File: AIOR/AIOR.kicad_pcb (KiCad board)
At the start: 2 copper layers, 85 x 56.5 mm, 35 parts, among them J1 Conn_01x06, J2 Conn_01x02, P1 CONN_02X20, P2 CONN_01X02, P3 CONN_01X04, P8 CONN_01X02, P9 CONN_01X04, U1 MCP2517FD, U3 P82B715, U4 SI8641-SOIC, Y1 4MHz

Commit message: wip
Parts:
- removed C6, C7, C8: 100nF, Capacitors_SMD:C_0805_HandSoldering
- removed J2: Conn_01x02, Pin_Headers:Pin_Header_Straight_1x02_Pitch2.54mm
- removed R4: 4k7, Resistors_SMD:R_0805_HandSolderingII
- removed R7: 120, Resistors_SMD:R_1206_HandSolderingII
- removed R8: 0, Resistors_SMD:R_0805_HandSolderingII
- removed R9: 50, Resistors_SMD:R_0805_HandSolderingII
- removed U3: P82B715, w_smd_dil:so-8
- added C10: 100nF, Capacitor_SMD:C_0805_2012Metric_Pad1.15x1.40mm_HandSolder, F.Cu at (109.6, 53.5)
- added C20: 100nF, Capacitor_SMD:C_0805_2012Metric_Pad1.15x1.40mm_HandSolder, F.Cu at (98.5, 63.2)
- added C21: 100nF, Capacitor_SMD:C_0805_2012Metric_Pad1.15x1.40mm_HandSolder, F.Cu at (126.4, 34.8)
- added C22: 10uF, Capacitor_SMD:C_Elec_5x5.8, F.Cu at (112.0, 45.6)
- added C23: 100nF, Capacitor_SMD:C_0805_2012Metric_Pad1.15x1.40mm_HandSolder, F.Cu at (121.6, 36.0)
- added C24: 100nF, Capacitor_SMD:C_0805_2012Metric_Pad1.15x1.40mm_HandSolder, F.Cu at (98.5, 66.1)
- added C25: 100nF, Capacitor_SMD:C_0805_2012Metric_Pad1.15x1.40mm_HandSolder, F.Cu at (138.3, 22.7)
- added C26: 100nF, Capacitor_SMD:C_0805_2012Metric_Pad1.15x1.40mm_HandSolder, F.Cu at (118.6, 43.0)
- added C27: 22pF, Capacitor_SMD:C_0805_2012Metric_Pad1.15x1.40mm_HandSolder, F.Cu at (121.6, 38.9)
- added C28: 22pF, Capacitor_SMD:C_0805_2012Metric_Pad1.15x1.40mm_HandSolder, F.Cu at (138.3, 19.7)
- added C29: 100nF, Capacitor_SMD:C_0805_2012Metric_Pad1.15x1.40mm_HandSolder, F.Cu at (147.6, 11.1)
- added C30: 100nF, Capacitor_SMD:C_0805_2012Metric_Pad1.15x1.40mm_HandSolder, F.Cu at (90.7, 67.7)
- added C31: 100nF, Capacitor_SMD:C_0805_2012Metric_Pad1.15x1.40mm_HandSolder, F.Cu at (126.4, 31.8)
- added C40: 100nF, Capacitor_SMD:C_0805_2012Metric_Pad1.15x1.40mm_HandSolder, F.Cu at (103.7, 55.1)
- added C41: 100nF, Capacitor_SMD:C_0805_2012Metric_Pad1.15x1.40mm_HandSolder, F.Cu at (145.4, 34.7)
- added C42: 100nF, Capacitor_SMD:C_0805_2012Metric_Pad1.15x1.40mm_HandSolder, F.Cu at (122.7, 60.7)
- added C43: 100nF, Capacitor_SMD:C_0805_2012Metric_Pad1.15x1.40mm_HandSolder, F.Cu at (114.8, 78.7)
- added C44: 100nF, Capacitor_SMD:C_0805_2012Metric_Pad1.15x1.40mm_HandSolder, F.Cu at (110.2, 78.7)
- added C45: 1nF, Capacitor_SMD:C_0805_2012Metric_Pad1.15x1.40mm_HandSolder, F.Cu at (133.4, 49.5)
- added C46: 100nF, Capacitor_SMD:C_0805_2012Metric_Pad1.15x1.40mm_HandSolder, F.Cu at (150.1, 31.8)
- added C70: 100nF, Capacitor_SMD:C_0805_2012Metric_Pad1.15x1.40mm_HandSolder, F.Cu at (128.6, 52.5)
- added C71: 1nF, Capacitor_SMD:C_0805_2012Metric_Pad1.15x1.40mm_HandSolder, F.Cu at (137.6, 43.3)
- added C72: 47pF, Capacitor_SMD:C_0805_2012Metric_Pad1.15x1.40mm_HandSolder, F.Cu at (122.7, 57.8)
- added C81: 100nF, Capacitor_SMD:C_0805_2012Metric_Pad1.15x1.40mm_HandSolder, F.Cu at (133.4, 46.6)
- added C82: 100nF, Capacitor_SMD:C_0805_2012Metric_Pad1.15x1.40mm_HandSolder, F.Cu at (119.2, 63.7)
- added C83: 100nF, Capacitor_SMD:C_0805_2012Metric_Pad1.15x1.40mm_HandSolder, F.Cu at (150.2, 28.8)
- added C84: 100nF, Capacitor_SMD:C_0805_2012Metric_Pad1.15x1.40mm_HandSolder, F.Cu at (114.4, 65.3)
- added C85: 100nF, Capacitor_SMD:C_0805_2012Metric_Pad1.15x1.40mm_HandSolder, F.Cu at (117.9, 60.7)
- added C86: 100nF, Capacitor_SMD:C_0805_2012Metric_Pad1.15x1.40mm_HandSolder, F.Cu at (137.6, 40.4)
- added C90: 100nF, Capacitor_SMD:C_0805_2012Metric_Pad1.15x1.40mm_HandSolder, F.Cu at (140.6, 37.4)
- added C91: 47pF, Capacitor_SMD:C_0805_2012Metric_Pad1.15x1.40mm_HandSolder, F.Cu at (140.7, 28.6)
- added C92: 47pF, Capacitor_SMD:C_0805_2012Metric_Pad1.15x1.40mm_HandSolder, F.Cu at (145.4, 37.7)
- added C93: 1nF, Capacitor_SMD:C_0805_2012Metric_Pad1.15x1.40mm_HandSolder, F.Cu at (126.3, 37.7)
- added C94: 1nF, Capacitor_SMD:C_0805_2012Metric_Pad1.15x1.40mm_HandSolder, F.Cu at (147.6, 14.1)
- added C95: 1nF, Capacitor_SMD:C_0805_2012Metric_Pad1.15x1.40mm_HandSolder, F.Cu at (108.4, 59.4)
- added C96: 560pF, Capacitor_SMD:C_0805_2012Metric_Pad1.15x1.40mm_HandSolder, F.Cu at (114.3, 53.5)
- added C97: 1nF, Capacitor_SMD:C_0805_2012Metric_Pad1.15x1.40mm_HandSolder, F.Cu at (152.3, 14.1)
- added C98: 1nF, Capacitor_SMD:C_0805_2012Metric_Pad1.15x1.40mm_HandSolder, F.Cu at (108.4, 56.5)
- added C99: 1nF, Capacitor_SMD:C_0805_2012Metric_Pad1.15x1.40mm_HandSolder, F.Cu at (147.8, 17.0)
- added D20: BAT43, Diode_SMD:D_SOD-323_HandSoldering, F.Cu at (85.8, 67.7)
- added D21: LED, LED_SMD:LED_0805_2012Metric_Pad1.15x1.40mm_HandSolder, F.Cu at (126.4, 28.8)
- added D70: LED, LED_SMD:LED_0805_2012Metric_Pad1.15x1.40mm_HandSolder, F.Cu at (109.6, 50.5)
- added D71: LED, LED_SMD:LED_0805_2012Metric_Pad1.15x1.40mm_HandSolder, F.Cu at (131.2, 28.3)
- added D90: 1N4148W, Diode_SMD:D_SOD-123, F.Cu at (104.3, 52.0)
- added D91: 1N4148W, Diode_SMD:D_SOD-123, F.Cu at (104.3, 48.6)
- added J20: Conn_01x04, Connector_PinHeader_2.54mm:PinHeader_1x04_P2.54mm_Vertical, F.Cu at (82.3, 29.8)
- added J30: Conn_01x01, Connector:Banana_Jack_1Pin, F.Cu at (167.1, 121.5)
- added J31: Conn_01x01, Connector:Banana_Jack_1Pin, F.Cu at (153.9, 121.4)
- added J50: Conn_01x02, Connector_PinHeader_2.54mm:PinHeader_1x02_P2.54mm_Vertical, F.Cu at (133.6, 20.6)
- added J70: Conn_01x01, Connector_PinHeader_2.54mm:PinHeader_1x01_P2.54mm_Vertical, F.Cu at (150.1, 38.5)
- added J81: Conn_01x06, Connector_PinHeader_2.54mm:PinHeader_1x06_P2.54mm_Horizontal, F.Cu at (132.8, 107.4)
- added J82: 5V 12V, Connector_PinHeader_2.54mm:PinHeader_1x03_P2.54mm_Vertical, F.Cu at (110.4, 34.8)
- added J90: Conn_01x03, Connector_PinHeader_2.54mm:PinHeader_1x03_P2.54mm_Vertical, F.Cu at (78.4, 42.0)
- added P50: Xpressnet, w_conn_jst-ph:s4b-ph-kl, F.Cu at (119.2, 11.8)
- added P60: Selectrix, w_conn_jst-ph:s4b-ph-kl, F.Cu at (102.4, 25.6)
- added P70: LOCONET, w_conn_jst-ph:s4b-ph-kl, F.Cu at (40.5, 74.0)
- added Q60: BC817, Package_TO_SOT_SMD:SOT-23_Handsoldering, F.Cu at (92.9, 64.0)
- added Q70: BC817, Package_TO_SOT_SMD:SOT-23_Handsoldering, F.Cu at (53.8, 74.7)
- added Q90: BC857, Package_TO_SOT_SMD:SOT-23_Handsoldering, F.Cu at (116.0, 39.3)
- added Q91: BC857, Package_TO_SOT_SMD:SOT-23_Handsoldering, F.Cu at (116.0, 34.7)
- added R20: 3k3, Resistor_SMD:R_0805_2012Metric_Pad1.15x1.40mm_HandSolder, F.Cu at (104.9, 66.9)
- added R21: 1k, Resistor_SMD:R_0805_2012Metric_Pad1.15x1.40mm_HandSolder, F.Cu at (147.8, 25.9)
- added R22: 3k3, Resistor_SMD:R_0805_2012Metric_Pad1.15x1.40mm_HandSolder, F.Cu at (119.1, 54.8)
- added R23: 3k3, Resistor_SMD:R_0805_2012Metric_Pad1.15x1.40mm_HandSolder, F.Cu at (123.4, 44.8)
- added R24: 18k, Resistor_SMD:R_0805_2012Metric_Pad1.15x1.40mm_HandSolder, F.Cu at (132.9, 40.7)
- added R25: 4k7, Resistor_SMD:R_0805_2012Metric_Pad1.15x1.40mm_HandSolder, F.Cu at (140.6, 34.5)
- added R30: 0, Resistor_SMD:R_0805_2012Metric_Pad1.15x1.40mm_HandSolder, F.Cu at (123.9, 50.7)
- added R31: 10k, Resistor_SMD:R_0805_2012Metric_Pad1.15x1.40mm_HandSolder, F.Cu at (152.5, 22.9)
- added R32: 3k3, Resistor_SMD:R_0805_2012Metric_Pad1.15x1.40mm_HandSolder, F.Cu at (113.2, 62.4)
- added R33: 4k7, Resistor_SMD:R_0805_2012Metric_Pad1.15x1.40mm_HandSolder, F.Cu at (123.9, 47.8)
- added R34: 100, Resistor_SMD:R_0805_2012Metric_Pad1.15x1.40mm_HandSolder, F.Cu at (132.9, 43.6)
- added R35: 100, Resistor_SMD:R_0805_2012Metric_Pad1.15x1.40mm_HandSolder, F.Cu at (145.5, 28.8)
- added R36: 4k7, Resistor_SMD:R_0805_2012Metric_Pad1.15x1.40mm_HandSolder, F.Cu at (109.7, 65.3)
- added R37: 0, Resistor_SMD:R_0805_2012Metric_Pad1.15x1.40mm_HandSolder, F.Cu at (123.9, 53.7)
- added R40: 470, Resistor_SMD:R_0805_2012Metric_Pad1.15x1.40mm_HandSolder, F.Cu at (128.6, 49.5)
- added R400: 3k3, Resistor_SMD:R_0805_2012Metric_Pad1.15x1.40mm_HandSolder, F.Cu at (154.9, 31.8)
- added R401: 3k3, Resistor_SMD:R_0805_2012Metric_Pad1.15x1.40mm_HandSolder, F.Cu at (147.8, 22.9)
- added R41: 3k3, Resistor_SMD:R_0805_2012Metric_Pad1.15x1.40mm_HandSolder, F.Cu at (152.5, 25.9)
- added R42: 470, Resistor_SMD:R_0805_2012Metric_Pad1.15x1.40mm_HandSolder, F.Cu at (145.4, 31.8)
- added R43: 3k3, Resistor_SMD:R_0805_2012Metric_Pad1.15x1.40mm_HandSolder, F.Cu at (128.6, 46.6)
- added R44: 1k, Resistor_SMD:R_0805_2012Metric_Pad1.15x1.40mm_HandSolder, F.Cu at (131.1, 37.7)
- added R45: 1k, Resistor_SMD:R_0805_2012Metric_Pad1.15x1.40mm_HandSolder, F.Cu at (138.3, 25.6)
- added R46: 1k, Resistor_SMD:R_0805_2012Metric_Pad1.15x1.40mm_HandSolder, F.Cu at (118.6, 46.0)
- added R47: 1k, Resistor_SMD:R_0805_2012Metric_Pad1.15x1.40mm_HandSolder, F.Cu at (152.3, 11.1)
- added R48: 0, Resistor_SMD:R_0805_2012Metric_Pad1.15x1.40mm_HandSolder, F.Cu at (123.4, 41.9)
- added R49: 0, Resistor_SMD:R_0805_2012Metric_Pad1.15x1.40mm_HandSolder, F.Cu at (119.1, 48.9)
- added R50: 470, Resistor_SMD:R_0805_2012Metric_Pad1.15x1.40mm_HandSolder, F.Cu at (100.2, 69.1)
- added R51: 470, Resistor_SMD:R_0805_2012Metric_Pad1.15x1.40mm_HandSolder, F.Cu at (103.7, 58.1)
- added R52: 120, Resistor_SMD:R_1206_3216Metric_Pad1.42x1.75mm_HandSolder, F.Cu at (104.4, 45.3)
- added R60: 27k, Resistor_SMD:R_0805_2012Metric_Pad1.15x1.40mm_HandSolder, F.Cu at (152.5, 17.0)
- added R61: 27k, Resistor_SMD:R_0805_2012Metric_Pad1.15x1.40mm_HandSolder, F.Cu at (128.6, 55.4)
- added R62: 120, Resistor_SMD:R_0805_2012Metric_Pad1.15x1.40mm_HandSolder, F.Cu at (147.8, 20.0)
- added R63: 1k, Resistor_SMD:R_0805_2012Metric_Pad1.15x1.40mm_HandSolder, F.Cu at (155.0, 28.8)
- added R700: 12, Resistor_SMD:R_1206_3216Metric_Pad1.42x1.75mm_HandSolder, F.Cu at (57.6, 69.2)
- added R701: 12, Resistor_SMD:R_1206_3216Metric_Pad1.42x1.75mm_HandSolder, F.Cu at (51.6, 69.2)
- added R702: 47k, Resistor_SMD:R_0805_2012Metric_Pad1.15x1.40mm_HandSolder, F.Cu at (133.4, 52.5)
- added R703: 150k, Resistor_SMD:R_0805_2012Metric_Pad1.15x1.40mm_HandSolder, F.Cu at (142.4, 40.6)
- added R71: 2k2, Resistor_SMD:R_0805_2012Metric_Pad1.15x1.40mm_HandSolder, F.Cu at (150.1, 34.7)
- added R72: 1k, Resistor_SMD:R_0805_2012Metric_Pad1.15x1.40mm_HandSolder, F.Cu at (138.1, 46.3)
- added R74: 240k, Resistor_SMD:R_0805_2012Metric_Pad1.15x1.40mm_HandSolder, F.Cu at (108.4, 62.4)
- added R75: 10k, Resistor_SMD:R_0805_2012Metric_Pad1.15x1.40mm_HandSolder, F.Cu at (113.2, 59.4)
- added R76: 1k, Resistor_SMD:R_0805_2012Metric_Pad1.15x1.40mm_HandSolder, F.Cu at (128.1, 43.6)
- added R77: 470, Resistor_SMD:R_0805_2012Metric_Pad1.15x1.40mm_HandSolder, F.Cu at (152.5, 20.0)
- added R78: 27k, Resistor_SMD:R_0805_2012Metric_Pad1.15x1.40mm_HandSolder, F.Cu at (140.6, 31.5)
- added R79: 39k, Resistor_SMD:R_0805_2012Metric_Pad1.15x1.40mm_HandSolder, F.Cu at (117.9, 57.8)
- added R81: 1k5, Resistor_SMD:R_0805_2012Metric_Pad1.15x1.40mm_HandSolder, F.Cu at (119.1, 51.9)
- added R90: 0, Resistor_SMD:R_0805_2012Metric_Pad1.15x1.40mm_HandSolder, F.Cu at (135.9, 34.5)
- added R91: 1M, Resistor_SMD:R_0805_2012Metric_Pad1.15x1.40mm_HandSolder, F.Cu at (113.2, 56.5)
- added R92: 2k2, Resistor_SMD:R_0805_2012Metric_Pad1.15x1.40mm_HandSolder, F.Cu at (128.1, 40.7)
- added R93: 3k3, Resistor_SMD:R_0805_2012Metric_Pad1.15x1.40mm_HandSolder, F.Cu at (135.9, 37.4)
- added R94: 8k2, Resistor_SMD:R_0805_2012Metric_Pad1.15x1.40mm_HandSolder, F.Cu at (123.9, 63.7)
- added R95: 8k2, Resistor_SMD:R_0805_2012Metric_Pad1.15x1.40mm_HandSolder, F.Cu at (127.4, 58.4)
- added R96: 3k3, Resistor_SMD:R_0805_2012Metric_Pad1.15x1.40mm_HandSolder, F.Cu at (138.1, 49.2)
- added TR30: 530x0c, Diverse:530x0C, F.Cu at (160.5, 109.7)
- added U2: ISO1050, Package_DIP:DIP-8_W8.89mm_SMDSocket_LongPads, F.Cu at (175.0, 85.0)
- added U20: L7833, Package_TO_SOT_SMD:TO-252-3_TabPin2, F.Cu at (90.7, 31.5)
- added U21: L7805, Package_TO_SOT_SMD:TO-252-3_TabPin2, F.Cu at (67.3, 55.4)
- added U22: DSPIC33EP128GM604, Package_QFP:LQFP-44_10x10mm_P0.8mm, F.Cu at (154.3, 96.5)
- added U23: Si8605, Package_SO:SOIC-16_3.9x9.9mm_P1.27mm, F.Cu at (146.6, 83.3)
- added U24: MCP2562, w_smd_dil:so-8, F.Cu at (174.5, 103.0)
- added U30: BTN8962, Package_TO_SOT_SMD:TO-263-7_TabPin8, F.Cu at (180.0, 118.5)
- added U31: BTN8962, Package_TO_SOT_SMD:TO-263-7_TabPin8, F.Cu at (141.3, 118.7)
- added U40: C8051F502, Package_QFP:LQFP-32_7x7mm_P0.8mm, F.Cu at (198.5, 82.0)
- added U41: ADUM1251, w_smd_dil:so-8, F.Cu at (186.5, 84.0)
- added U42: MCP2561-E-SN, w_smd_dil:so-8, F.Cu at (137.6, 14.0)
- added U50: MAX3072E, w_smd_dil:so-8, F.Cu at (205.0, 95.0)
- added U70: LM393, w_smd_dil:so-8, F.Cu at (128.3, 22.5)
- added U81: L7805, Package_TO_SOT_SMD:TO-252-3_TabPin2, F.Cu at (98.7, 19.5)
- added U82: SI8641-SOIC, w_smd_dil:so-16, F.Cu at (140.1, 95.8)
- added U83: 4504, w_smd_dil:so-16, F.Cu at (140.1, 104.9)
- added U90: SAA6579, Package_SO:SOP-16_7.5x10.4mm_P1.27mm, F.Cu at (195.6, 109.7)
- added Y20: 8MHz, w_crystal:crystal_hc-49s, B.Cu at (164.0, 96.0)
- added Y90: 4MHz, w_crystal:crystal_hc-49s, F.Cu at (204.7, 109.5)
- C1: value 22pF -> 100nF; footprint Capacitors_SMD:C_0805_HandSoldering -> Capacitor_SMD:C_0805_2012Metric_Pad1.15x1.40mm_HandSolder
- C2, C4, C5: footprint Capacitors_SMD:C_0805_HandSoldering -> Capacitor_SMD:C_0805_2012Metric_Pad1.15x1.40mm_HandSolder
- C3: value 100nF -> 22pF; footprint Capacitors_SMD:C_0805_HandSoldering -> Capacitor_SMD:C_0805_2012Metric_Pad1.15x1.40mm_HandSolder
- J1: value Conn_01x06 -> Conn_01x02; footprint Pin_Headers:Pin_Header_Angled_1x06_Pitch2.54mm -> Connector_PinHeader_2.54mm:PinHeader_1x02_P2.54mm_Vertical; moved to F.Cu
- P2, P8: footprint Pin_Headers:Pin_Header_Angled_1x02 -> Connector_PinHeader_2.54mm:PinHeader_1x02_P2.54mm_Vertical; moved to F.Cu
- P3, P9, Y1: moved to F.Cu
- R1, R10, R11, R12, R13, R2: footprint Resistors_SMD:R_0805_HandSolderingII -> Resistor_SMD:R_0805_2012Metric_Pad1.15x1.40mm_HandSolder
- R3: value 4k7 -> 120; footprint Resistors_SMD:R_0805_HandSolderingII -> Resistor_SMD:R_0805_2012Metric_Pad1.15x1.40mm_HandSolder
- U4: value SI8641-SOIC -> P82B715; footprint w_smd_dil:so-16 -> w_smd_dil:so-8
- moved J1 111.1 mm to (142.9, 12.0), turned to 0 degrees
- moved Y1 102.1 mm to (98.8, 12.6)
- moved G*** 91.1 mm to (245.7, 83.4)
- moved P3 84.9 mm to (66.8, 63.9), turned to 0 degrees
- moved C5 81.7 mm to (143.0, 18.3), turned to 0 degrees
- moved C2 79.4 mm to (143.0, 21.3)
- moved C4 68.0 mm to (131.1, 31.8), turned to 0 degrees
- moved C1 67.6 mm to (131.1, 34.8), turned to 0 degrees
- moved R1 66.8 mm to (143.0, 24.2), turned to 0 degrees
- moved R3 66.1 mm to (103.3, 64.0), turned to 0 degrees
- moved R13 65.9 mm to (71.6, 80.5), turned to 0 degrees
- moved P8 64.9 mm to (121.7, 29.6), turned to 0 degrees
- moved P2 63.9 mm to (99.0, 55.5), turned to 0 degrees
- moved R11 59.8 mm to (136.0, 28.6), turned to 0 degrees
- moved R2 57.7 mm to (95.4, 69.1)
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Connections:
- net /INT0 renamed Net-(U1-Pad9)
- net /INT1 renamed Net-(U1-Pad8)
- C1 pad 1: Net-(C1-Pad1) -> +3V3
- C3 pad 1: +3V3 -> Net-(C3-Pad1)
- C5 pad 1: +5V -> +5VA
- J1 pad 1: VDDA -> /GPIO27
- J1 pad 2: Net-(J1-Pad2) -> /GPIO22
- P1 pad 16: /INT0_ -> Net-(P1-Pad16)
- P1 pad 18: /INT1_ -> Net-(P1-Pad18)
- P1 pad 37: Net-(P1-Pad37) -> /_C2D
- P1 pad 39: Net-(P1-Pad39) -> GND
- P1 pad 40: Net-(P1-Pad40) -> /_C2CK
- P3 pad 2: +5V -> +5VA
- P3 pad 3: /CANH -> /CANL
- P3 pad 4: /CANL -> /CANH
- R1 pad 2: /INT -> /CS0
- R2 pad 2: /CS0 -> /INT
- R3 pad 1: +3V3 -> Net-(P2-Pad1)
- R3 pad 2: /INT0_ -> /CANH
- U1 pad 5: Net-(C1-Pad1) -> Net-(C3-Pad1)
- U4 pad 1: +3V3 -> (no net)
- U4 pad 2: GND -> Net-(P9-Pad4)
- U4 pad 3: /GPIO22 -> /SCL
- U4 pad 4: /GPIO27 -> GND
- U4 pad 5: /GPIO17 -> (no net)
- U4 pad 6: /GPIO4 -> /SDA
- U4 pad 7: Net-(U4-Pad7) -> Net-(P9-Pad3)
- U4 pad 8: GND -> +3V3
- Y1 pad 1: Net-(C1-Pad1) -> Net-(C3-Pad1)
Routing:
- removed copper zone on B.Cu, net GND
- removed copper zone on F.Cu, net GND
- removed copper zone on B.Cu, net GNDA
- removed copper zone on F.Cu, net GNDA
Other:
- board text removed: "5V"
- board text removed: "CAN Term"
- board text removed: "CANH"
- board text removed: "CANL"
- board text removed: "GND"
- board text removed: "GPIO17"
- board text removed: "GPIO22"
- board text removed: "GPIO27"
- board text removed: "GPIO4"
- board text removed: "I2C"
- board text removed: "I2C PWR"
- board text removed: "SCL"
- board text removed: "SDA"

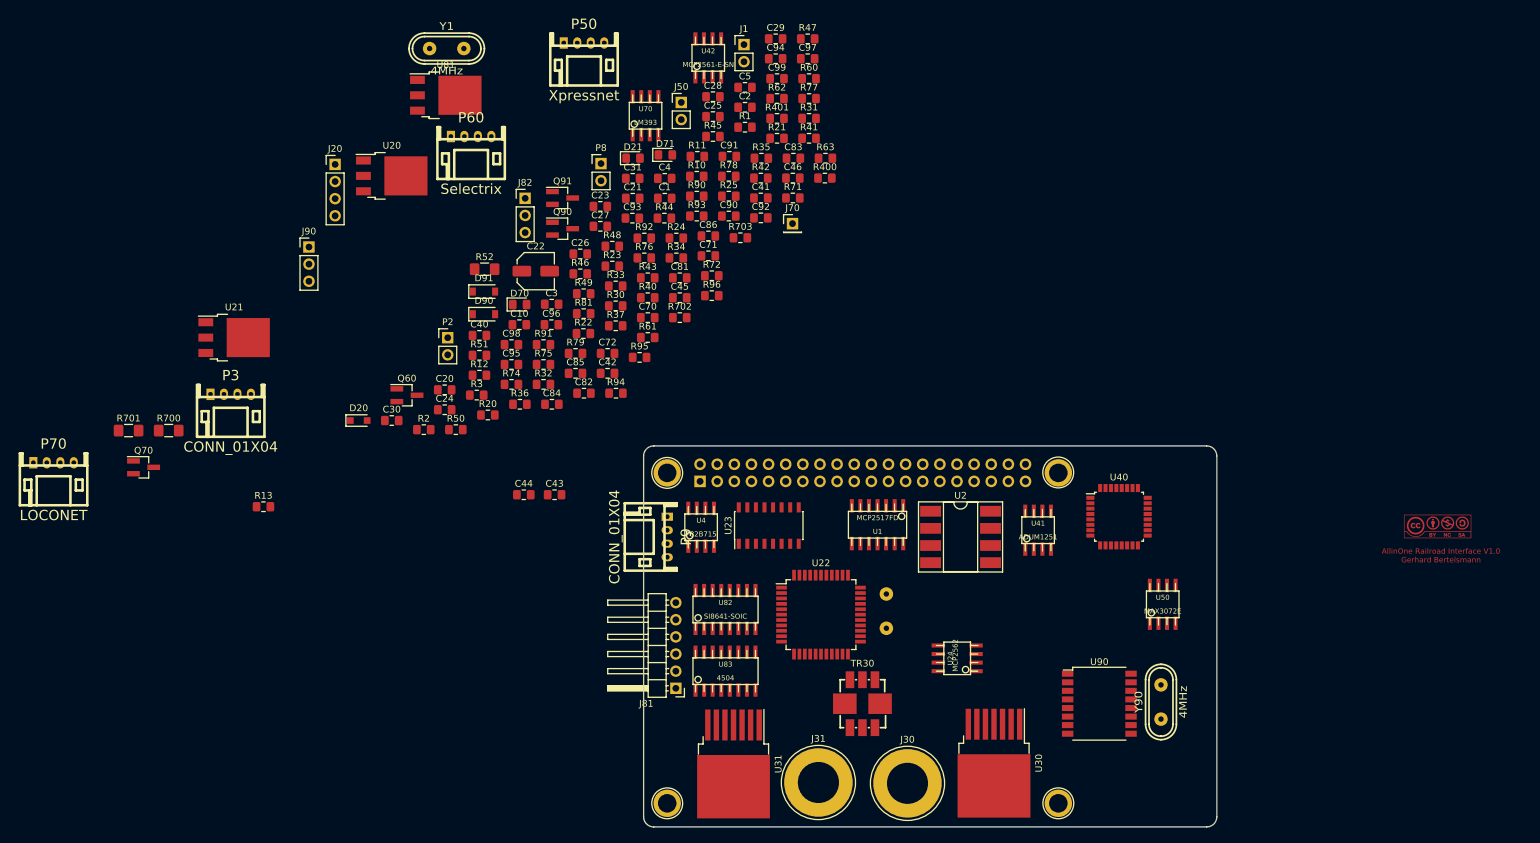
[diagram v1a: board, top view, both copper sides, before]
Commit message: use existing BTN89082 lib
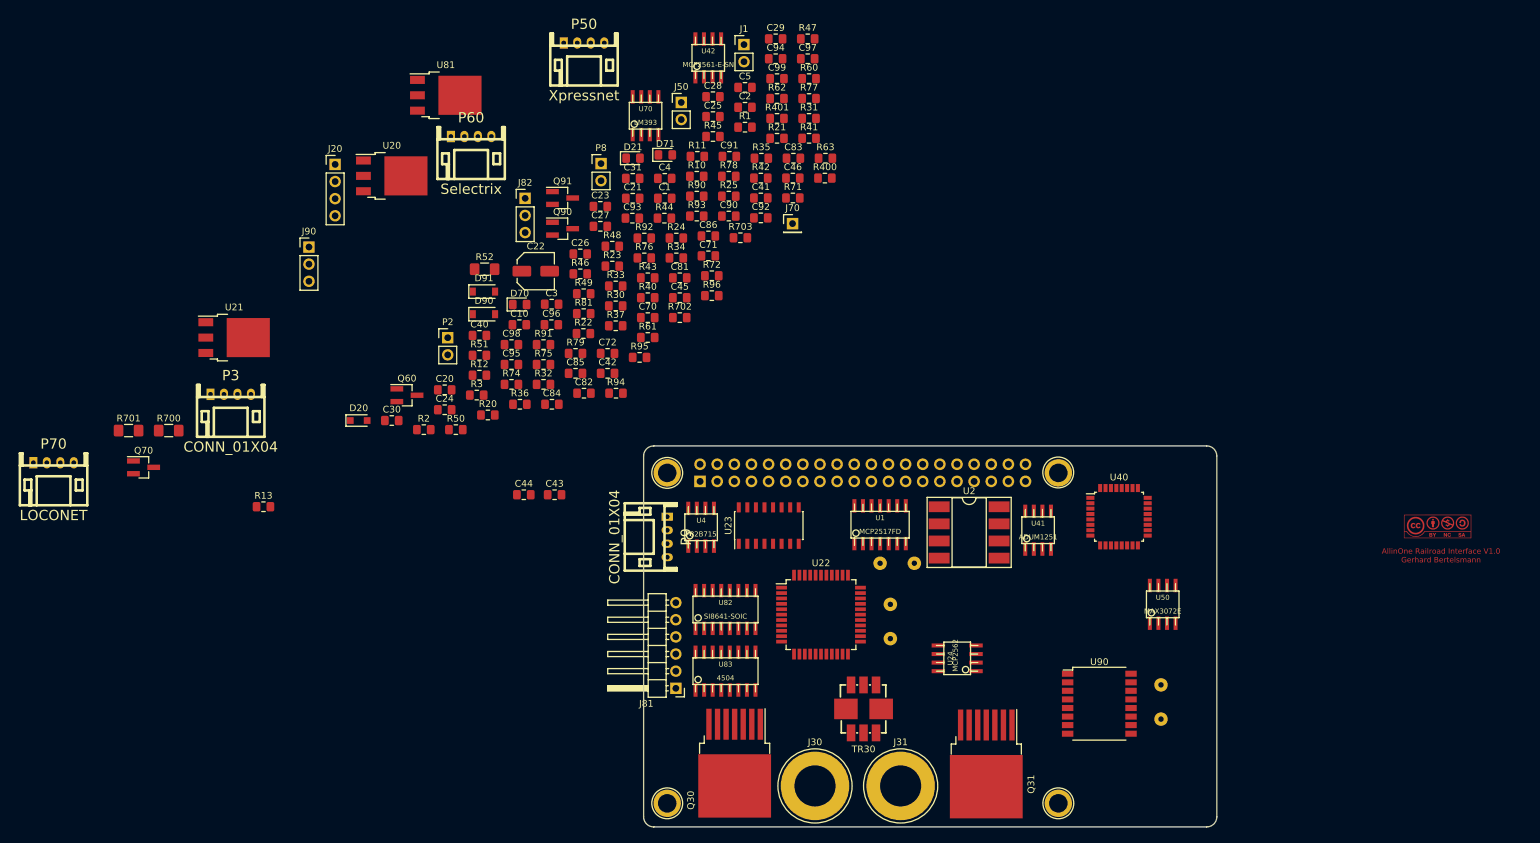
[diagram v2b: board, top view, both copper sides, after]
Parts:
- removed U30, U31: BTN8962, Package_TO_SOT_SMD:TO-263-7_TabPin8
- added Q30: BTN8982TA, Package_TO_SOT_SMD:TO-263-7_TabPin8, F.Cu at (141.5, 118.5)
- added Q31: BTN8982TA, Package_TO_SOT_SMD:TO-263-7_TabPin8, F.Cu at (178.8, 118.7)
- Y1, Y90: moved to B.Cu
- moved Y1 101.4 mm to (165.6, 88.9)
- moved J30 13.7 mm to (153.4, 121.9)
- moved J31 12.2 mm to (166.1, 121.9)
- moved Y20 1.65 mm to (164.6, 97.5)
- moved U2 1.44 mm to (176.3, 84.3)
- moved TR30 0.79 mm to (160.6, 110.5), turned to 180 degrees
- moved U1 0.38 mm to (163.1, 83.2), turned to 0 degrees
- turned Y90 to 270 degrees

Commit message: wip
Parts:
- J30, J31: value Conn_01x01 -> Conn_01x02; footprint Connector:Banana_Jack_1Pin -> w_conn_mkds:mkds_1,5-2
- P3: value CONN_01X04 -> CAN; footprint w_conn_jst-ph:s4b-ph-kl -> w_conn_jst-ph:b4b-ph-kl
- P50, P60, P70: footprint w_conn_jst-ph:s4b-ph-kl -> w_conn_jst-ph:b4b-ph-kl
- P9: moved to B.Cu
- moved P70 213.3 mm to (253.0, 54.9)
- moved Q70 184.4 mm to (237.7, 60.5)
- moved R701 184.4 mm to (235.5, 55.0)
- moved R700 184.4 mm to (241.5, 55.0)
- moved P60 165.2 mm to (239.8, 117.3)
- moved Q60 153.1 mm to (242.3, 97.5)
- moved J90 136.4 mm to (193.0, 115.8)
- moved U70 127.8 mm to (247.9, 67.6)
- moved Q91 127.6 mm to (207.3, 124.0)
- moved R62 126.7 mm to (238.8, 108.2)
- moved Q90 120.1 mm to (201.2, 124.0)
- moved R60 120.0 mm to (237.2, 102.1)
- moved D91 119.1 mm to (196.1, 124.5)
- moved C97 116.5 mm to (203.2, 118.9)
- moved C94 116.3 mm to (198.1, 118.9)
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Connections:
- J30 pad 1: /HBL -> GNDA
- J31 pad 1: /HBR -> /HBL

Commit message: wip
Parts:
- removed J1: Conn_01x02, Connector_PinHeader_2.54mm:PinHeader_1x02_P2.54mm_Vertical
- G***: moved to B.Cu
- P50: value Xpressnet -> XPN
- P60: value Selectrix -> SLX
- P70: value LOCONET -> LCN
- moved G*** 118.2 mm to (132.5, 117.2), turned to 270 degrees
- moved C98 116.4 mm to (205.7, 120.4), turned to 90 degrees
- moved C96 115.1 mm to (209.8, 117.9)
- moved C95 113.2 mm to (206.2, 116.3), turned to 90 degrees
- moved C93 110.0 mm to (206.2, 113.3)
- moved R93 108.8 mm to (203.2, 122.9)
- moved R79 104.3 mm to (198.1, 124.5)
- moved R51 104.3 mm to (205.7, 79.2), turned to 90 degrees
- moved D70 101.6 mm to (201.2, 94.5)
- moved R92 101.3 mm to (190.2, 120.7)
- moved C91 100.1 mm to (187.2, 117.2), turned to 90 degrees
- moved D90 99.8 mm to (188.5, 105.7), turned to 90 degrees
- moved C72 97.8 mm to (207.3, 106.7), turned to 270 degrees
- moved D71 97.4 mm to (193.5, 103.3)
- moved R46 96.7 mm to (205.2, 88.9)
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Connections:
- P1 pad 13: /GPIO27 -> Net-(P1-Pad13)
- P1 pad 15: /GPIO22 -> Net-(P1-Pad15)
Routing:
- net /MOSI: track 0.00 -> 0.70 mm

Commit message: let's have a look if all components fit on the board
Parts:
- C22: footprint Capacitor_SMD:C_Elec_5x5.8 -> Capacitor_Tantalum_SMD:CP_EIA-6032-20_AVX-F_Pad2.25x2.35mm_HandSolder
- J20: footprint Connector_PinHeader_2.54mm:PinHeader_1x04_P2.54mm_Vertical -> Connector_PinHeader_1.27mm:PinHeader_1x04_P1.27mm_Vertical
- P8: value CONN_01X02 -> Conn_01x02
- P9: value CONN_01X04 -> Conn_01x04
- U2: footprint Package_DIP:DIP-8_W8.89mm_SMDSocket_LongPads -> w_smd_dil:mdip_8
- U42: value MCP2561-E-SN -> MCP2561
- moved R90 101.8 mm to (201.8, 112.0)
- moved C70 97.2 mm to (201.5, 116.7)
- moved R75 95.9 mm to (194.1, 110.9), turned to 90 degrees
- moved R91 94.0 mm to (190.2, 110.4)
- moved R44 88.6 mm to (205.6, 85.7), turned to 270 degrees
- moved R43 87.7 mm to (201.8, 94.9)
- moved C31 86.2 mm to (177.8, 109.9), turned to 180 degrees
- moved R702 85.1 mm to (201.5, 103.4), turned to 270 degrees
- moved R35 83.4 mm to (182.0, 110.0)
- moved R48 80.2 mm to (194.6, 78.6), turned to 90 degrees
- moved R49 79.0 mm to (192.3, 78.6), turned to 90 degrees
- moved R40 78.3 mm to (193.0, 94.1)
- moved C27 74.9 mm to (168.4, 97.3)
- moved C45 74.3 mm to (201.9, 78.2)
- moved R25 74.0 mm to (144.9, 108.3), turned to 180 degrees
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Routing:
- net /INT: track 0.00 -> 12.8 mm, vias 0 -> 1

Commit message: optimize placement - wip
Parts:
- moved C21 24.7 mm to (143.4, 117.1), turned to 0 degrees
- moved C20 22.4 mm to (137.6, 110.6), turned to 180 degrees
- moved C28 21.2 mm to (149.7, 102.1), turned to 180 degrees
- moved C83 21.0 mm to (138.0, 107.8), turned to 0 degrees
- moved D21 20.0 mm to (169.2, 99.8)
- moved R21 19.5 mm to (167.1, 99.8), turned to 270 degrees
- moved C29 19.2 mm to (150.1, 93.6), turned to 180 degrees
- moved R61 19.1 mm to (156.5, 106.5), turned to 270 degrees
- moved C27 18.9 mm to (149.7, 100.2), turned to 180 degrees
- moved C25 18.5 mm to (150.2, 96.6), turned to 180 degrees
- moved C82 18.2 mm to (129.9, 107.2), turned to 0 degrees
- moved D20 17.9 mm to (156.0, 84.3)
- moved Y20 17.9 mm to (150.7, 101.3), turned to 90 degrees
- moved J20 17.8 mm to (161.3, 105.9), turned to 90 degrees
- moved R25 17.5 mm to (150.0, 91.6), turned to 0 degrees
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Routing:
- net /INT: track 12.8 -> 0.00 mm, vias 1 -> 0
- net /MOSI: track 0.70 -> 0.00 mm

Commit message: wip
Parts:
- moved R3 7.01 mm to (172.2, 112.8)
- moved R12 5.08 mm to (137.5, 87.4), turned to 180 degrees
- moved U24 5.02 mm to (171.7, 104.8), turned to 270 degrees
- moved R11 3.66 mm to (141.6, 87.4), turned to 180 degrees
- moved R10 2.41 mm to (143.7, 82.9)
- moved R13 2.41 mm to (141.6, 82.9)
- moved R81 1.52 mm to (143.8, 97.3)
- moved U83 1.31 mm to (140.8, 92.4)
- moved C85 1.15 mm to (137.6, 97.4)
- moved C83 0.52 mm to (137.6, 107.7)
- moved U4 0.28 mm to (138.1, 82.1)
- moved U23 0.06 mm to (150.0, 82.5)
